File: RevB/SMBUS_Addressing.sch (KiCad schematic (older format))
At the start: 18 parts, among them J5 Conn_02x04_Odd_Even, SW1 SW_DIP_x03, SW3 SW_DIP_x03, U3 4051

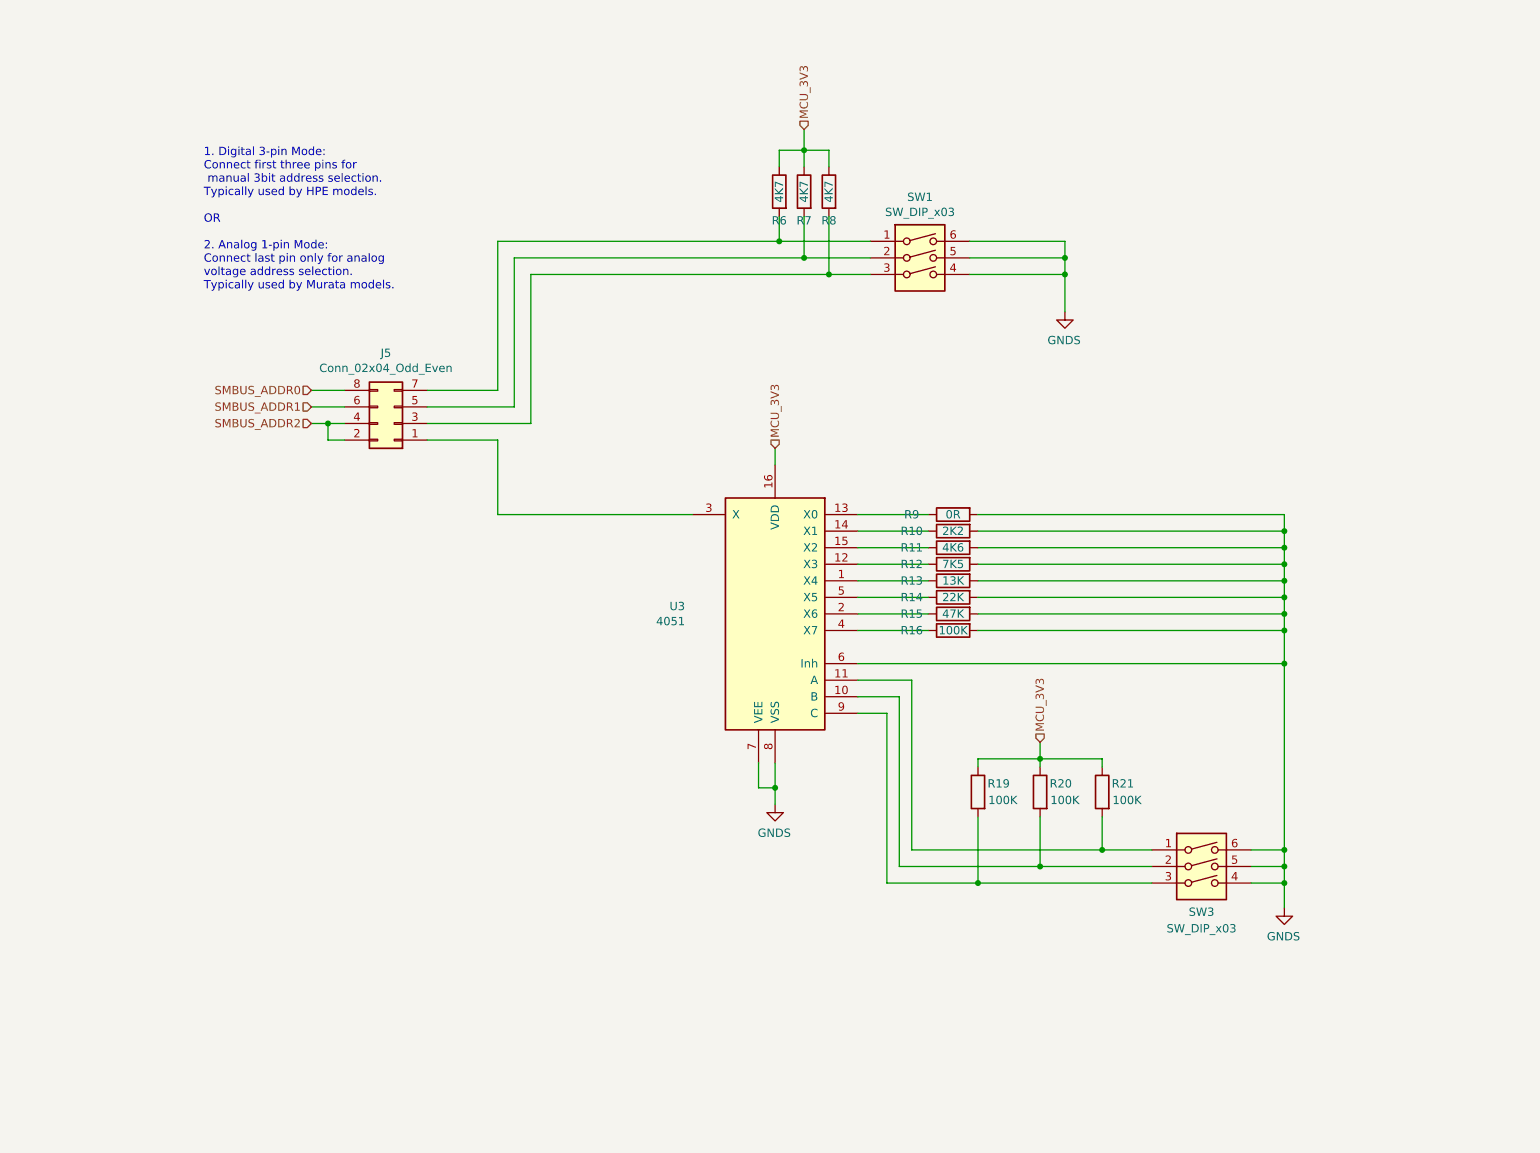
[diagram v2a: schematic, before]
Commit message: hw update
- changed third dip switch to cd4066 and spdt slide switch
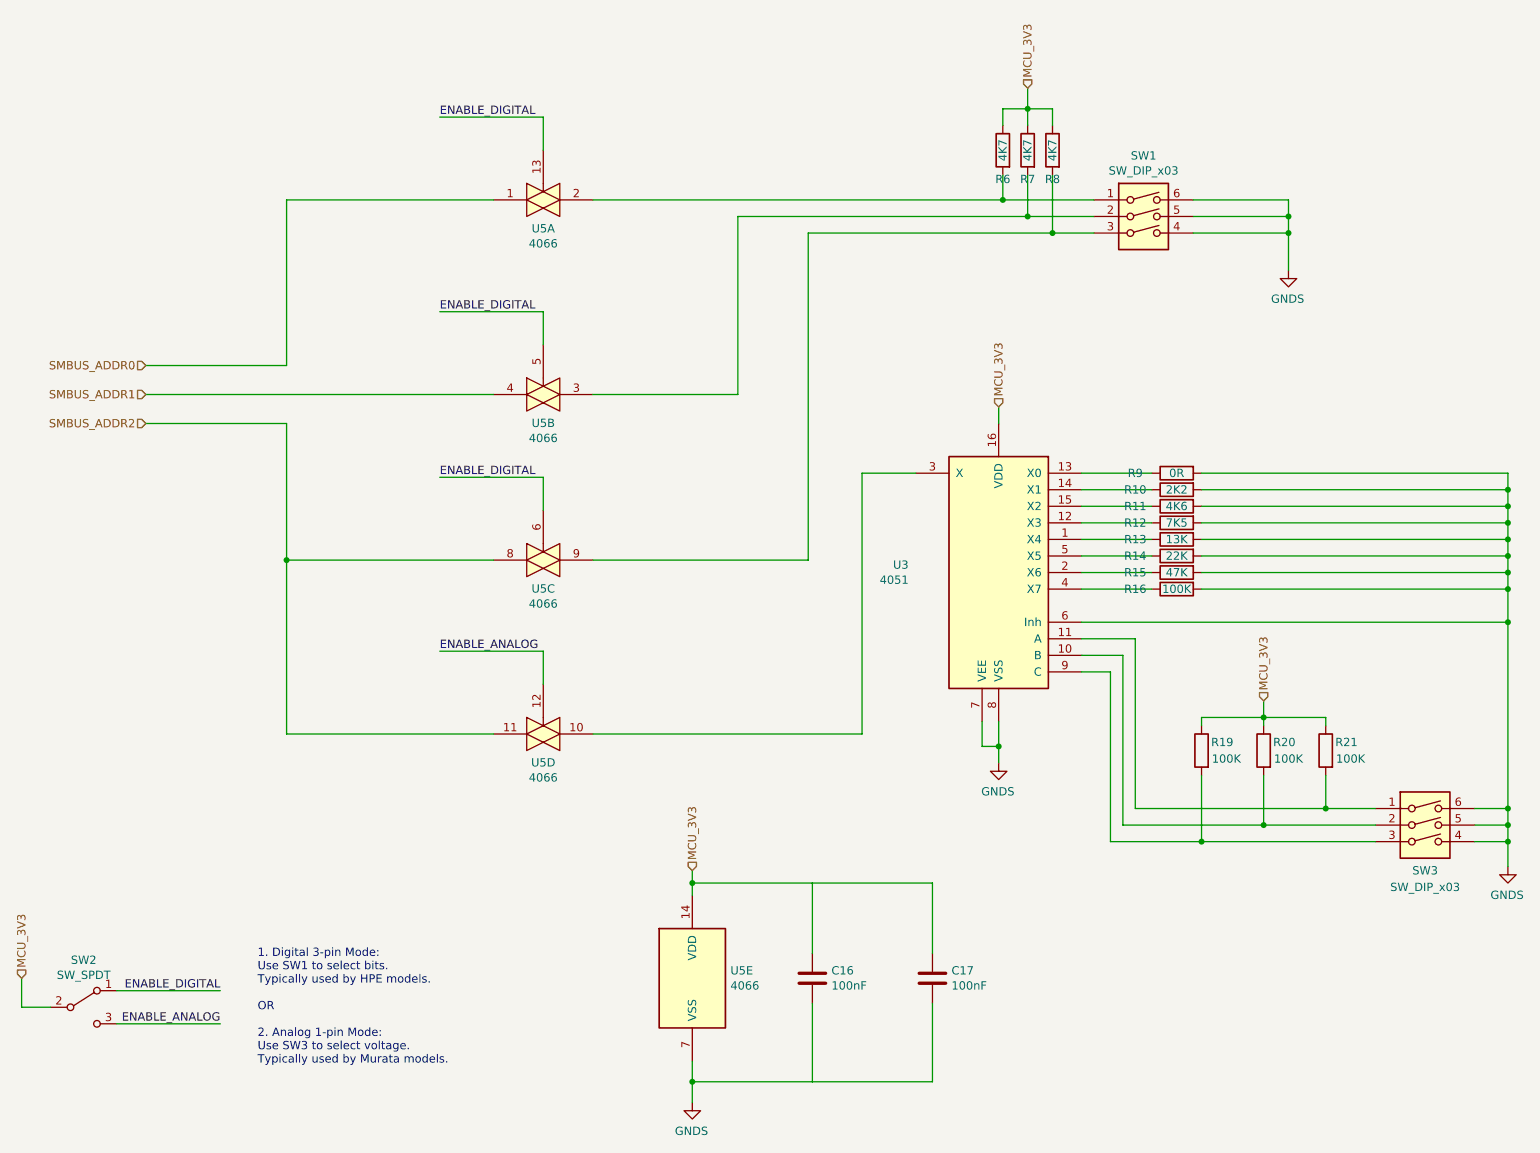
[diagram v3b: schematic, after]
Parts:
- removed J5: Conn_02x04_Odd_Even, Connector_PinHeader_2.54mm:PinHeader_2x04_P2.54mm_Vertical, symbol Connector_Generic:Conn_02x04_Odd_Even
- added C16, C17: 100nF, Capacitor_SMD:C_0805_2012Metric_Pad1.15x1.40mm_HandSolder, symbol Device:C
- added SW2: SW_SPDT, JS_Series_Sub-Miniature_Slide_Switches:JS102011SAQN, symbol Switch:SW_SPDT
- added U5: 4066, Package_SO:SOIC-14_3.9x8.7mm_P1.27mm, symbol 4xxx:4066
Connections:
- net GNDS: now also C16.2, C17.2, U5.7 (VSS)
- net MCU_3V3: now also C16.1, C17.1, SW2.2 (B), U5.14 (VDD)
- net SMBUS_ADDR0: now also U5.1
- net SMBUS_ADDR1: now also U5.4
- net SMBUS_ADDR2: now also U5.11, U5.8
- net at U3.3 (X): now also U5.10
- net at R8.2, SW1.3: now also U5.9
- net at R7.2, SW1.2: now also U5.3
- net at R6.2, SW1.1: now also U5.2
- new net ENABLE_ANALOG: SW2.3 (C), U5.12
- new net ENABLE_DIGITAL: SW2.1 (A), U5.13, U5.5, U5.6
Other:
- note added: "1. Digital 3-pin Mode:\nUse SW1 to select bits.\nTypically used by HPE models.\n\nOR\n\n2. Analog 1-pin Mode:\nUse SW3 to select voltage.\nTypically used by Murata models."
- note removed: "1. Digital 3-pin Mode:\nConnect first three pins for\n manual 3bit address selection.\nTypically used by HPE models.\n\nOR\n\n2. Analog 1-pin Mode:\nConnect last pin only for analog \nvoltage address selection.\nTypically used by Murata models."
- moved on the sheet: R10, R11, R12, R13, R14, R15, R16, R19, R20, R21, R6, R7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

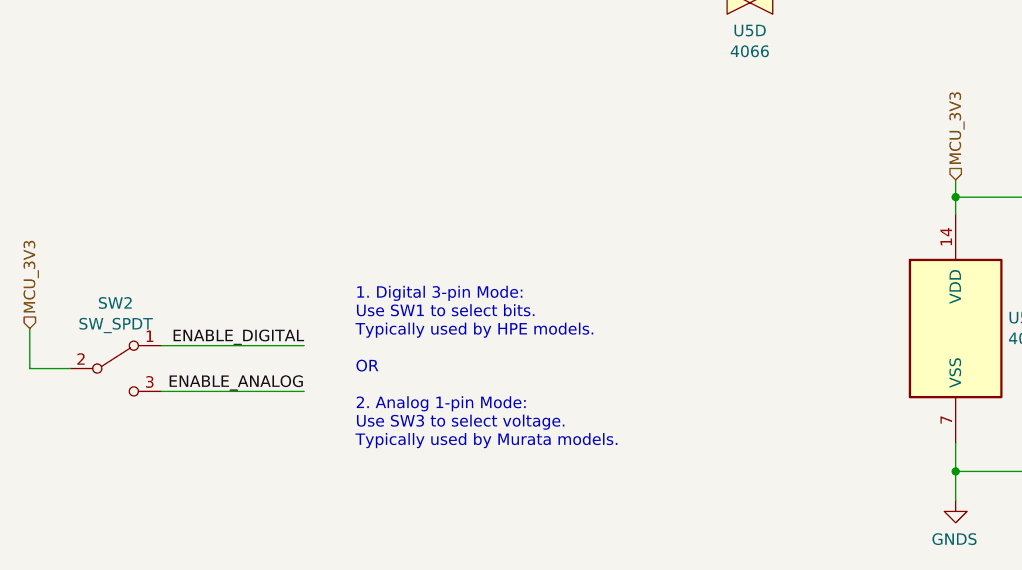
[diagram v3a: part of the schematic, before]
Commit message: hw update
updated revb. Added board connectors for device stacking
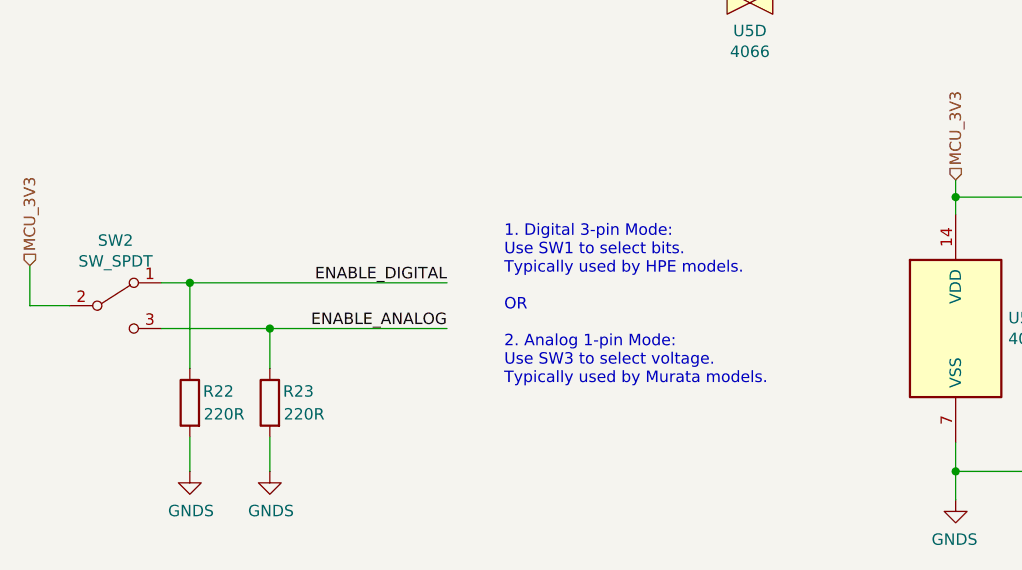
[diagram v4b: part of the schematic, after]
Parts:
- added R22, R23: 220R, Resistor_SMD:R_0805_2012Metric_Pad1.15x1.40mm_HandSolder, symbol Device:R
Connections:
- net ENABLE_ANALOG: now also R23.1
- net ENABLE_DIGITAL: now also R22.1
- net GNDS: now also R22.2, R23.2
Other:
- moved on the sheet: SW2
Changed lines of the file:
@@
 Wire Wire Line
 	6900 3125 6900 3225
-Text Notes 2425 7100 0    50   ~ 0
+Text Notes 3075 6825 0    50   ~ 0
 1. Digital 3-pin Mode:\nUse SW1 to select bits.\nTypically used by HPE models.\n\nOR\n\n2. Analog 1-pin Mode:\nUse SW3 to select voltage.\nTypically used by Murata models.
 $Comp
@@
 L Switch:SW_SPDT SW2
 U 1 1 5F43DA46
-P 1375 6750
-F 0 "SW2" H 1375 7035 50  0000 C CNN
-F 1 "SW_SPDT" H 1375 6944 50  0000 C CNN
-F 2 "JS_Series_Sub-Miniature_Slide_Switches:JS102011SAQN" H 1375 6750 50  0001 C CNN
-F 3 "https://docs.rs-online.com/6ed6/0900766b815f51c4.pdf" H 1375 6750 50  0001 C CNN
-	1    1375 6750
-	1    0    0    -1
-$EndComp
-Text HLabel 1000 6575 1    50   Input ~ 0
+P 1375 6475
+F 0 "SW2" H 1375 6760 50  0000 C CNN
+F 1 "SW_SPDT" H 1375 6669 50  0000 C CNN
+F 2 "JS_Series_Sub-Miniature_Slide_Switches:JS102011SAQN" H 1375 6475 50  0001 C CNN
+F 3 "https://docs.rs-online.com/6ed6/0900766b815f51c4.pdf" H 1375 6475 50  0001 C CNN
+	1    1375 6475
+	1    0    0    -1
+$EndComp
+Text HLabel 1000 6300 1    50   Input ~ 0
 MCU_3V3
 Wire Wire Line
-	1000 6575 1000 6750
-Wire Wire Line
-	1000 6750 1175 6750
-Wire Wire Line
-	1575 6650 2200 6650
-Wire Wire Line
-	1575 6850 2200 6850
-Text Label 2200 6850 2    50   ~ 0
+	1000 6300 1000 6475
+Wire Wire Line
+	1575 6375 1700 6375
+Wire Wire Line
+	1575 6575 2050 6575
+Text Label 2825 6575 2    50   ~ 0
 ENABLE_ANALOG
-Text Label 2200 6650 2    50   ~ 0
+Text Label 2825 6375 2    50   ~ 0
 ENABLE_DIGITAL
 Wire Wire Line
@@
 Wire Wire Line
 	6500 7200 6500 6725
+$Comp
+L Device:R R?
+U 1 1 5F313317
+P 1700 6900
+AR Path="/5EFF0F4B/5F313317" Ref="R?"  Part="1"
+AR Path="/5F02F4E9/5F313317" Ref="R?"  Part="1"
+AR Path="/5F02F4E9/5F3E7977/5F313317" Ref="R?"  Part="1"
+AR Path="/5F02F4E9/5F4AA6E5/5F313317" Ref="R22"  Part="1"
+F 0 "R22" H 1575 6950 50  0000 C CNN
+F 1 "220R" H 1550 6850 50  0000 C CNN
+F 2 "Resistor_SMD:R_0805_2012Metric_Pad1.15x1.40mm_HandSolder" V 1630 6900 50  0001 C CNN
+F 3 "~" H 1700 6900 50  0001 C CNN
+	1    1700 6900
+	-1   0    0    -1
+$EndComp
+Wire Wire Line
+	1700 6750 1700 6375
+Wire Wire Line
+	1700 7050 1700 7200
+$Comp
+L power:GNDS #PWR018
+U 1 1 5F31D6EA
+P 1700 7200
+F 0 "#PWR018" H 1700 6950 50  0001 C CNN
+F 1 "GNDS" H 1705 7027 50  0000 C CNN
+F 2 "" H 1700 7200 50  0001 C CNN
+F 3 "" H 1700 7200 50  0001 C CNN
+	1    1700 7200
+	1    0    0    -1
+$EndComp
+Wire Wire Line
+	1000 6475 1175 6475
+Connection ~ 1700 6375
+Wire Wire Line
+	1700 6375 2825 6375
+$Comp
+L Device:R R?
+U 1 1 5F350823
+P 2050 6900
+AR Path="/5EFF0F4B/5F350823" Ref="R?"  Part="1"
+AR Path="/5F02F4E9/5F350823" Ref="R?"  Part="1"
+AR Path="/5F02F4E9/5F3E7977/5F350823" Ref="R?"  Part="1"
+AR Path="/5F02F4E9/5F4AA6E5/5F350823" Ref="R23"  Part="1"
+F 0 "R23" H 1925 6950 50  0000 C CNN
+F 1 "220R" H 1900 6850 50  0000 C CNN
+F 2 "Resistor_SMD:R_0805_2012Metric_Pad1.15x1.40mm_HandSolder" V 1980 6900 50  0001 C CNN
+F 3 "~" H 2050 6900 50  0001 C CNN
+	1    2050 6900
+	-1   0    0    -1
+$EndComp
+Wire Wire Line
+	2050 6750 2050 6575
+Wire Wire Line
+	2050 7050 2050 7200
+$Comp
+L power:GNDS #PWR019
+U 1 1 5F35082B
+P 2050 7200
+F 0 "#PWR019" H 2050 6950 50  0001 C CNN
+F 1 "GNDS" H 2055 7027 50  0000 C CNN
+F 2 "" H 2050 7200 50  0001 C CNN
+F 3 "" H 2050 7200 50  0001 C CNN
+	1    2050 7200
+	1    0    0    -1
+$EndComp
+Connection ~ 2050 6575
+Wire Wire Line
+	2050 6575 2825 6575
 $EndSCHEMATC

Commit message: hw update
revb layout completed
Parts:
- SW2: footprint JS_Series_Sub-Miniature_Slide_Switches:JS102011SAQN -> Connector_PinHeader_2.54mm:PinHeader_1x03_P2.54mm_Vertical
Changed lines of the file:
@@
 F 0 "SW2" H 1375 6760 50  0000 C CNN
 F 1 "SW_SPDT" H 1375 6669 50  0000 C CNN
-F 2 "JS_Series_Sub-Miniature_Slide_Switches:JS102011SAQN" H 1375 6475 50  0001 C CNN
+F 2 "Connector_PinHeader_2.54mm:PinHeader_1x03_P2.54mm_Vertical" H 1375 6475 50  0001 C CNN
 F 3 "https://docs.rs-online.com/6ed6/0900766b815f51c4.pdf" H 1375 6475 50  0001 C CNN
 	1    1375 6475
